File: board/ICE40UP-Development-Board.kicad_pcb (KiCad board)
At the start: 4 copper layers, 41.9 x 20.3 mm, 61 parts, among them X1 USB4105-GF-A, X2 Conn_01x16, X3 Conn_01x16, X4 Tag-Connect, Y1 48MHz

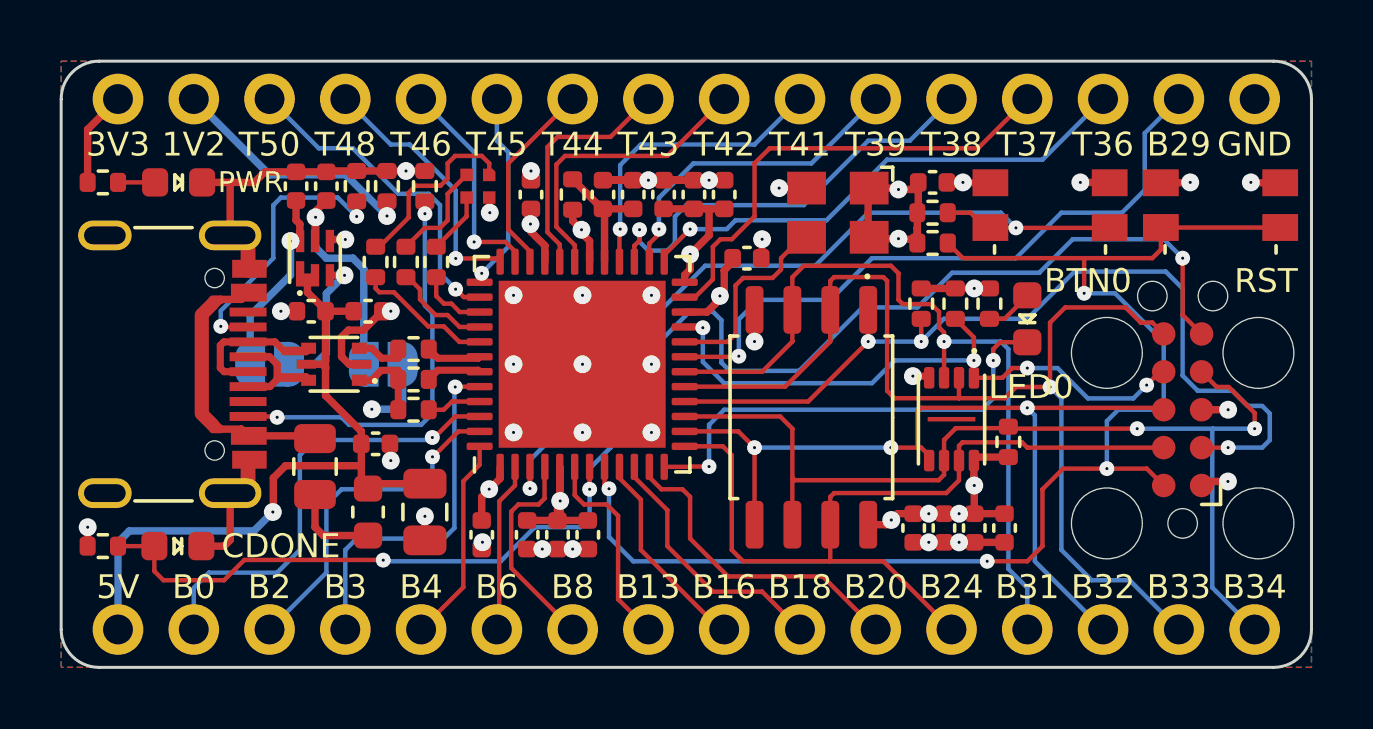
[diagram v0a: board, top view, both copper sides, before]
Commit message: change led resistor values, again
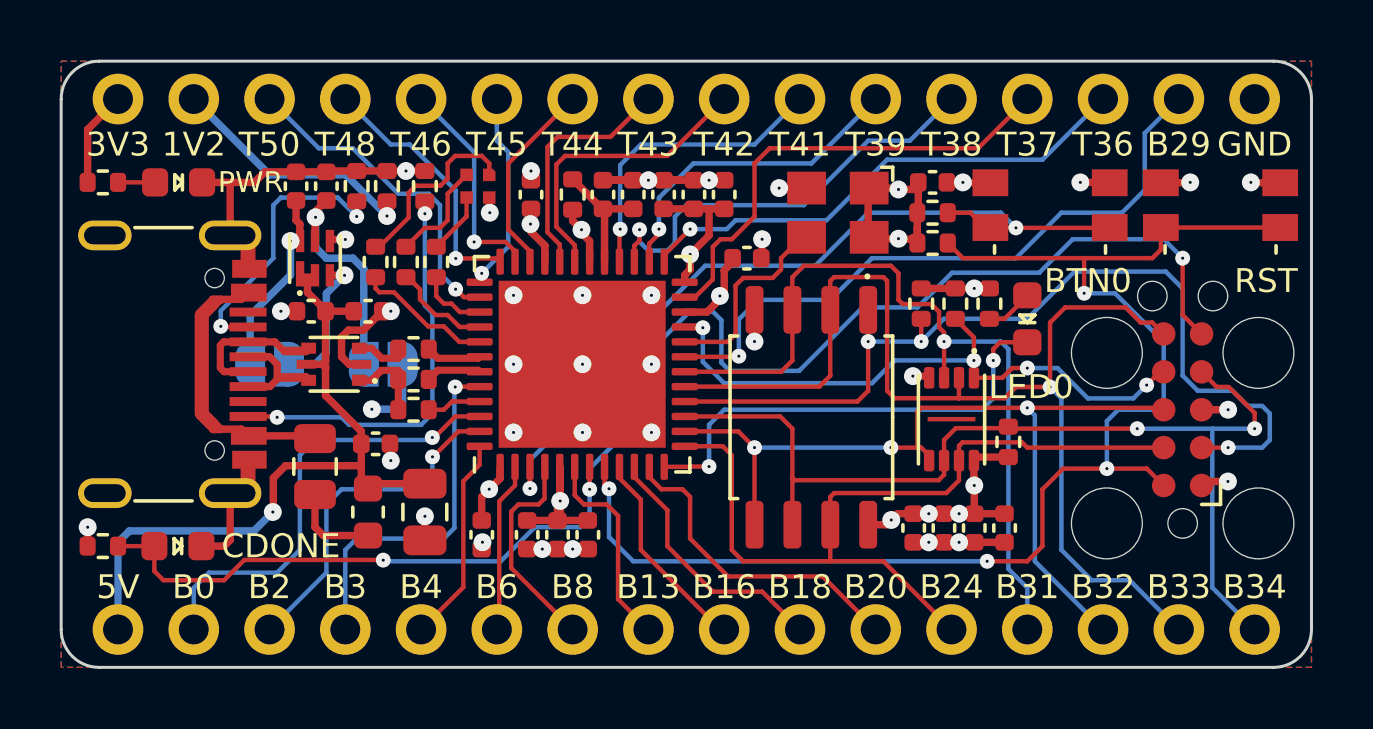
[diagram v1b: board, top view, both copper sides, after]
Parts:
- F1: value Fuse_Small -> 200mA
- R16: value 10k -> 1k
- R17: value 10k -> 33k
- R18: value 10k -> 2k2
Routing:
- net FLASH_~{SS}: track 30.3 -> 31.2 mm
- net SPI_SI: track 36.8 -> 37.5 mm

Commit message: update rgb led resistors; change capacitor placement
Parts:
- R13, R14, R15: value 100R -> 470R
- moved C15 2.03 mm to (74.9, 83.6)
- moved R12 1.02 mm to (74.9, 82.5)
- moved R11 1.02 mm to (74.9, 81.5)
- turned S1 to 0 degrees
- turned S2 to 0 degrees
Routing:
- net GND: track 42.9 -> 48.5 mm, vias 32 -> 30
- net ~{RST}: track 46.7 -> 49.0 mm
- net ~{CONF}_I: track 29.3 -> 27.7 mm
- net IOB_29b: track 22.0 -> 21.4 mm

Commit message: add QSPI nWP & nHOLD pull-up resistors
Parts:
- added R7: 10k, Resistor_SMD:R_0402_1005Metric, F.Cu at (78.5, 90.9)
- added R9: 10k, Resistor_SMD:R_0402_1005Metric, F.Cu at (78.5, 93.1)
- moved R1 0.70 mm to (77.5, 90.9)
- moved C10 0.13 mm to (76.5, 93.1)
- moved C8 0.13 mm to (77.5, 93.1)
- renumbered C22 to C21, C21 to C22, C4 to C3, C3 to C4, R8 to R10, R9 to R11, R10 to R12, R11 to R13, R12 to R14, R13 to R15, R14 to R16, R15 to R17, R16 to R18, R17 to R19, R4 to R2, R18 to R20, R2 to R3, R3 to R4, R7 to R8, V6 to V5, V5 to V6
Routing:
- net +3V3: track 38.3 -> 40.5 mm, vias 15 -> 16
- net ~{RST}: track 49.0 -> 50.7 mm
- net SPI_~{WP}: track 27.0 -> 28.5 mm, vias 1 -> 2
- net SPI_SCK: track 34.2 -> 35.6 mm
- net SPI_~{HOLD}: track 28.2 -> 29.3 mm
- net GND: track 48.5 -> 48.6 mm, vias 30 -> 31
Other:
- board text added: "v1.1"
- board text removed: "v1.0"
